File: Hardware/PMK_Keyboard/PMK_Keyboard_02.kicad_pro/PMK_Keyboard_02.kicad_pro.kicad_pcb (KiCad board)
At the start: 2 copper layers, 145 x 111.8 mm, 101 parts, among them J201 PSoM_ESP32S2_Carrier_Board, J202 PSoM_ESP32S2_Carrier_Board, J301 USB4510-03-1-A, J302 Conn_01x02, J303 S2B-PH-SM4-TB, J304 Conn_02x05_Top_Bottom, SW301 450405020524, SW401 SW_Push, SW402 SW_Push, SW403 SW_Push, SW404 SW_Push, SW405 SW_Push, SW406 SW_Push, SW407 SW_Push, SW408 SW_Push, SW409 SW_Push, SW410 SW_Push, SW411 SW_Push, SW412 SW_Push, SW413 SW_Push, SW414 SW_Push, SW415 SW_Push, SW416 SW_Push, SW417 SW_Push, SW418 SW_Push, SW419 SW_Push, SW420 SW_Push, SW421 SW_Push, SW422 SW_Push, SW423 SW_Push, SW424 SW_Push, SW425 SW_Push, SW426 SW_Push, SW427 SW_Push, SW428 SW_Push, SW429 SW_Push, SW430 RIC11-22S10D5S-TH, U401 SN74HC165PWR, U402 SN74HC165PWR, U403 SN74HC165PWR, U404 SN74HC165PWR, U405 SN74LVC2G04DBVRG4

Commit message: working on routing
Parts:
- C401, C402, C403, R401, R402, R403, R404: moved to B.Cu
- moved R405 99.6 mm to (205.7, 137.3), turned to 180 degrees
- moved R406 97.6 mm to (205.7, 136.0), turned to 180 degrees
- moved C403 89.9 mm to (211.8, 136.9)
- moved C402 89.5 mm to (211.2, 133.3), turned to 90 degrees
- moved C401 86.3 mm to (216.9, 133.3), turned to 90 degrees
- moved R401 85.7 mm to (215.3, 133.3), turned to -90 degrees
- moved R403 85.2 mm to (212.9, 133.3), turned to -90 degrees
- moved R404 84.7 mm to (212.1, 133.3), turned to 90 degrees
- moved R402 84.0 mm to (216.0, 133.3), turned to 90 degrees
- moved TP206 53.6 mm to (238.0, 92.8)
- moved TP207 53.6 mm to (238.0, 96.4)
- moved TP203 40.9 mm to (238.1, 89.5)
- moved TP208 36.6 mm to (238.1, 86.7)
- moved TP202 36.3 mm to (238.0, 84.2)
- moved TP201 36.1 mm to (238.0, 78.5)
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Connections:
- J201 pad 29: /200- PSoM/A -> /200- PSoM/DB_A
- J201 pad 31: /200- PSoM/B -> /200- PSoM/DB_B
- J202 pad 29: /200- PSoM/A -> /200- PSoM/DB_A
- J202 pad 31: /200- PSoM/B -> /200- PSoM/DB_B
- R401 pad 1: /200- PSoM/A -> /400- Shift Register - Switch/A
- R402 pad 2: /200- PSoM/A -> /400- Shift Register - Switch/A
- R403 pad 1: /200- PSoM/B -> /400- Shift Register - Switch/B
- R404 pad 2: /200- PSoM/B -> /400- Shift Register - Switch/B
- R405 pad 1: /200- PSoM/A -> /400- Shift Register - Switch/DB_A
- R405 pad 2: /400- Shift Register - Switch/31 -> /400- Shift Register - Switch/30
- R406 pad 1: /200- PSoM/B -> /400- Shift Register - Switch/DB_B
- R406 pad 2: /400- Shift Register - Switch/32 -> /400- Shift Register - Switch/31
- SW430 pad A: /200- PSoM/A -> /400- Shift Register - Switch/A
- SW430 pad B: /200- PSoM/B -> /400- Shift Register - Switch/B
- SW430 pad S2: /400- Shift Register - Switch/30 -> /400- Shift Register - Switch/32
- U405 pad 4: /200- PSoM/B -> /400- Shift Register - Switch/DB_B
- U405 pad 6: /200- PSoM/A -> /400- Shift Register - Switch/DB_A
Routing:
- net /200- PSoM/SR_CE: track 27.3 -> 64.8 mm, vias 2 -> 0
- net /200- PSoM/SPI_MISO: track 0.00 -> 24.6 mm, vias 0 -> 2
- net /400- Shift Register - Switch/B: track 0.00 -> 14.2 mm
- net /400- Shift Register - Switch/32: track 7.26 -> 20.6 mm
- net /200- PSoM/SPI_MOSI: track 0.00 -> 13.0 mm, vias 0 -> 1
- net /400- Shift Register - Switch/31: track 5.56 -> 15.2 mm
- net /400- Shift Register - Switch/A: track 0.00 -> 7.86 mm
- net /400- Shift Register - Switch/F_A: track 0.00 -> 7.25 mm, vias 0 -> 1
- net /200- PSoM/BATTERY_TEMP: track 0.00 -> 6.30 mm
- net Net-(J303-Pin_1): track 23.0 -> 28.5 mm, vias 2 -> 3
- net /400- Shift Register - Switch/DB_A: track 0.00 -> 4.55 mm
- net /400- Shift Register - Switch/DB_B: track 0.00 -> 4.34 mm
- net /400- Shift Register - Switch/F_B: track 0.00 -> 4.11 mm, vias 0 -> 1
- net /200- PSoM/SPI_CLK: track 86.5 -> 90.6 mm, vias 3 -> 1
- net /400- Shift Register - Switch/30: track 15.8 -> 12.4 mm
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
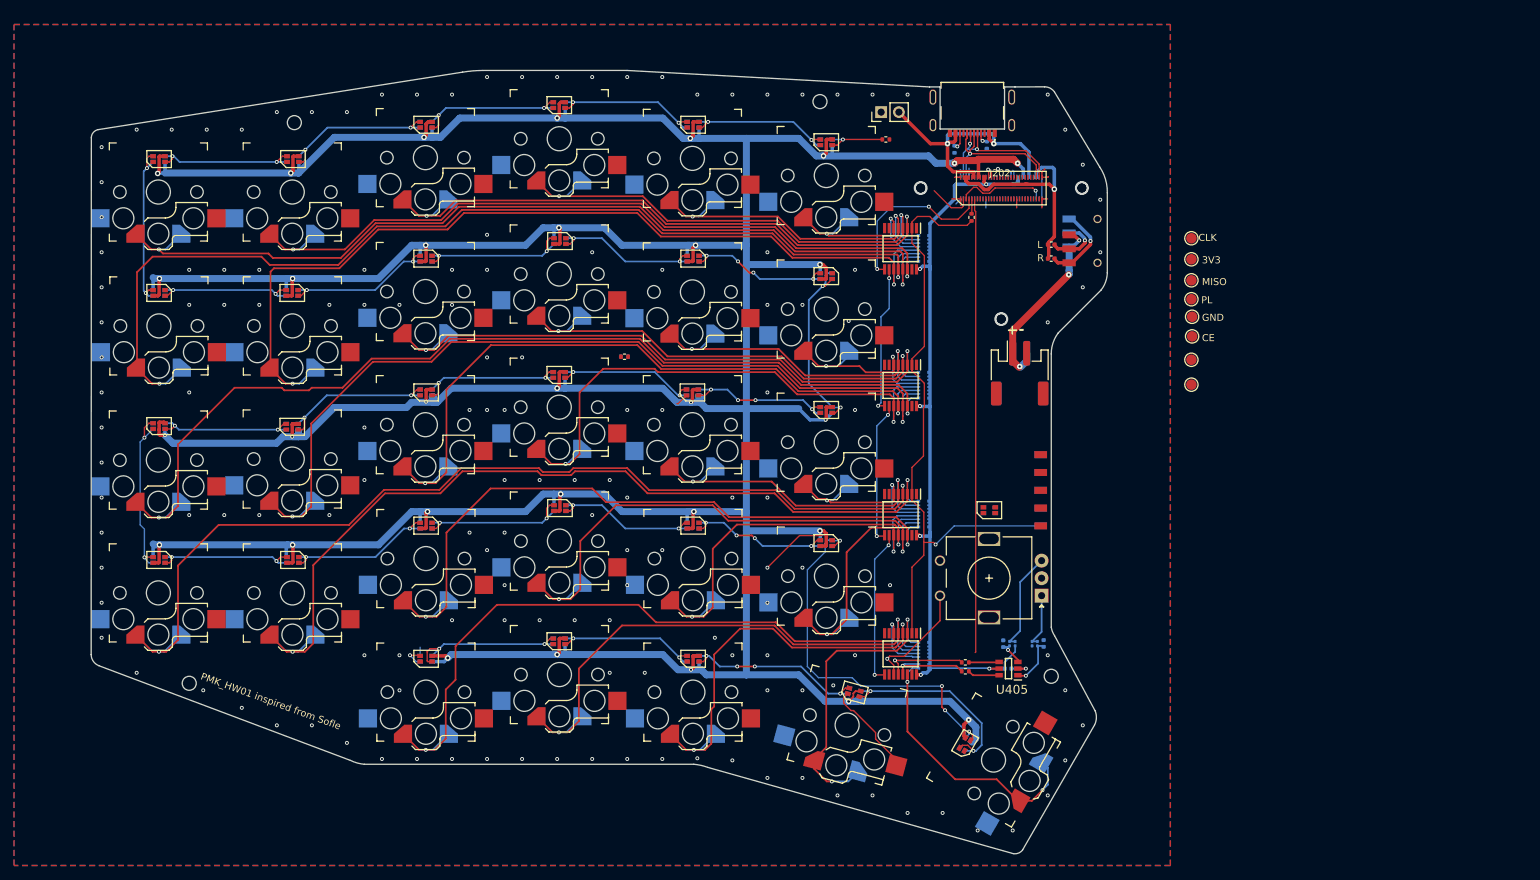
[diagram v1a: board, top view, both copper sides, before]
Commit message: updated key switch to kailh v2
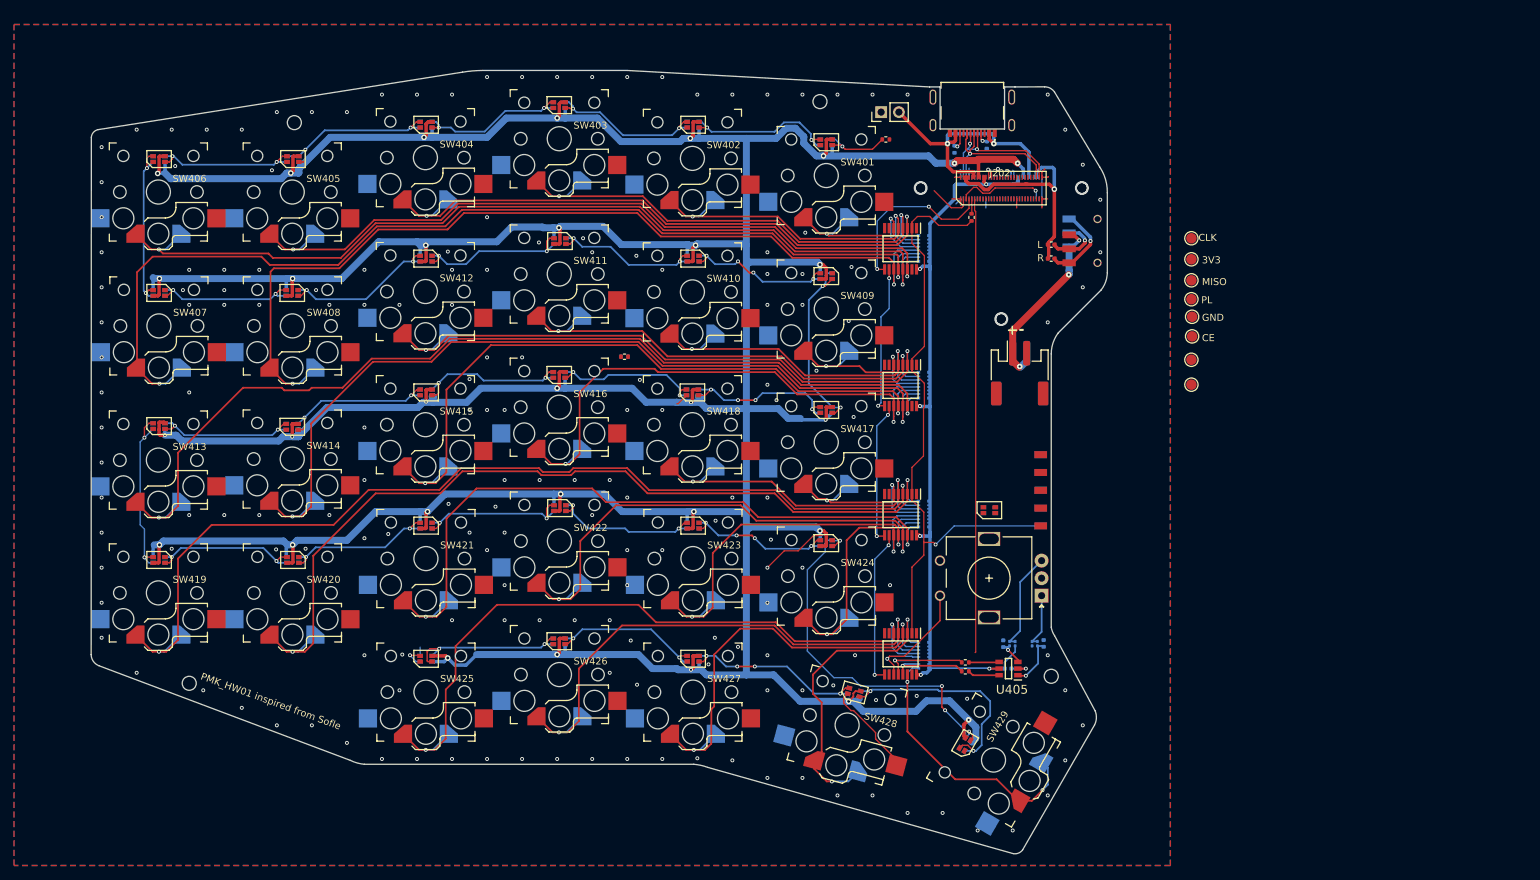
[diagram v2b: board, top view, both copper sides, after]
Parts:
- SW401, SW402, SW403, SW404, SW405, SW406, SW407, SW408, SW409, SW410, SW411, SW412, SW413, SW414, SW415, SW416, SW417, SW418, SW419, SW420, SW421, SW422, SW423, SW424, SW425, SW426, SW427, SW428, SW429: footprint Component_lib:Kailh_socket_PG1350_reversible -> Component_lib:Kailh_socket_PG1350_reversible_V1V2
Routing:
- net VDD: track 724.6 -> 732.4 mm
- net Net-(D525-DO): track 29.4 -> 33.2 mm
- net GND: track 57.0 -> 58.9 mm, vias 151 -> 181
- net /500- LEDs/LED_13_14: track 22.2 -> 23.8 mm
- net Net-(D524-DO): track 54.2 -> 52.9 mm
- net /400- Shift Register - Switch/21: track 99.5 -> 100.7 mm
- net Net-(D514-DO): track 21.7 -> 22.8 mm
- net Net-(D501-DO): track 21.6 -> 22.7 mm
- net Net-(D522-DO): track 21.8 -> 22.9 mm
- net Net-(D508-DO): track 22.2 -> 23.3 mm
- net Net-(D527-DO): track 21.5 -> 22.5 mm
- net Net-(D519-DO): track 21.0 -> 22.1 mm
- net /400- Shift Register - Switch/28: track 44.0 -> 45.1 mm
- net Net-(D509-DO): track 22.3 -> 23.3 mm
- net Net-(D502-DO): track 21.8 -> 22.8 mm
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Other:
- board text removed: "s5"
- board text removed: "s6"

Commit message: routing ongoing
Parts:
- J201: moved to F.Cu
- J202: moved to B.Cu
- J304: value Conn_02x05_Top_Bottom -> FH12-12S-0.5SH_55_; footprint Component_lib:PMK_Side_Conn_F -> Component_lib:FH12-12S-0.5SH_55_
- moved J304 13.0 mm to (205.0, 105.3)
- moved R202 2.44 mm to (204.2, 72.3), turned to 180 degrees
- moved J303 1.65 mm to (213.4, 93.1)
- turned J201 to 180 degrees
- turned J202 to 0 degrees
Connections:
- J201 pad 13: /200- PSoM/GP_CE -> /200- PSoM/SDA
- J201 pad 17: /200- PSoM/INT -> /200- PSoM/PL
- J201 pad 21: unconnected-(J201-IO10-Pad21) -> /200- PSoM/DR
- J201 pad 23: /200- PSoM/PL -> /200- PSoM/GP_CE
- J201 pad 25: /200- PSoM/DR -> /200- PSoM/GPIO1
- J201 pad 27: /200- PSoM/GP_CE -> /200- PSoM/GPIO2
- J201 pad 29: /200- PSoM/DB_A -> /200- PSoM/GPIO3
- J201 pad 31: /200- PSoM/DB_B -> /200- PSoM/DB_A
- J201 pad 33: /200- PSoM/LED_MOSI_ESP -> /200- PSoM/DB_B
- J201 pad 39: unconnected-(J201-IO21-Pad39) -> /200- PSoM/LED_MOSI_ESP
- J202 pad 13: /200- PSoM/GP_CE -> /200- PSoM/SDA
- J202 pad 17: /200- PSoM/INT -> /200- PSoM/PL
- J202 pad 21: unconnected-(J202-IO10-Pad21) -> /200- PSoM/DR
- J202 pad 23: /200- PSoM/PL -> /200- PSoM/GP_CE
- J202 pad 25: /200- PSoM/DR -> /200- PSoM/GPIO1
- J202 pad 27: /200- PSoM/GP_CE -> /200- PSoM/GPIO2
- J202 pad 29: /200- PSoM/DB_A -> /200- PSoM/GPIO3
- J202 pad 31: /200- PSoM/DB_B -> /200- PSoM/DB_A
- J202 pad 33: /200- PSoM/LED_MOSI_ESP -> /200- PSoM/DB_B
- J202 pad 39: unconnected-(J202-IO21-Pad39) -> /200- PSoM/LED_MOSI_ESP
- J304 pad 1: /200- PSoM/DR -> /200- PSoM/SPI_CLK
- J304 pad 10: /200- PSoM/SPI_CLK -> /200- PSoM/SDA
- J304 pad 2: /200- PSoM/GP_CE -> /200- PSoM/SPI_MISO
- J304 pad 3: /200- PSoM/SCL -> /200- PSoM/GP_CE
- J304 pad 4: /200- PSoM/INT -> /200- PSoM/DR
- J304 pad 5: GND -> /200- PSoM/SPI_MOSI
- J304 pad 6: +3V3 -> /200- PSoM/GPIO1
- J304 pad 7: /200- PSoM/SR_CE -> /200- PSoM/GPIO2
- J304 pad 8: /200- PSoM/SPI_MOSI -> /200- PSoM/GPIO3
- J304 pad 9: /200- PSoM/SPI_MISO -> /200- PSoM/SCL
- R405 pad 1: /400- Shift Register - Switch/DB_A -> /200- PSoM/DB_A
- R406 pad 1: /400- Shift Register - Switch/DB_B -> /200- PSoM/DB_B
- U405 pad 4: /400- Shift Register - Switch/DB_B -> /200- PSoM/DB_B
- U405 pad 6: /400- Shift Register - Switch/DB_A -> /200- PSoM/DB_A
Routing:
- net /200- PSoM/BATTERY_TEMP: track 6.30 -> 62.2 mm, vias 0 -> 4
- net /200- PSoM/SR_CE: track 64.8 -> 21.4 mm, vias 0 -> 2
- net /200- PSoM/SCL: track 0.00 -> 40.3 mm, vias 0 -> 2
- net /200- PSoM/SDA: track 0.00 -> 39.4 mm, vias 0 -> 2
- net /200- PSoM/GPIO3: track 0.00 -> 39.3 mm
- net /200- PSoM/SPI_MOSI: track 13.0 -> 52.0 mm, vias 1 -> 3
- net /200- PSoM/GPIO2: track 0.00 -> 38.6 mm
- net /200- PSoM/DR: track 0.00 -> 38.5 mm
- net /200- PSoM/GPIO1: track 0.00 -> 38.0 mm
- net /200- PSoM/GP_CE: track 0.00 -> 37.9 mm
- net /200- PSoM/SPI_MISO: track 24.6 -> 54.9 mm, vias 2 -> 4
- net /200- PSoM/LED_MOSI_ESP: track 0.00 -> 23.2 mm, vias 0 -> 2
- net /200- PSoM/PL: track 0.00 -> 13.0 mm, vias 0 -> 3
- net +3V3: track 110.9 -> 122.0 mm, vias 6 -> 7
- net /400- Shift Register - Switch/DB_A: track 4.55 -> 0.00 mm
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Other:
- board text added: "+ -"
- board text removed: "+-"
